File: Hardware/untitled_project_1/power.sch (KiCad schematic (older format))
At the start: 29 parts

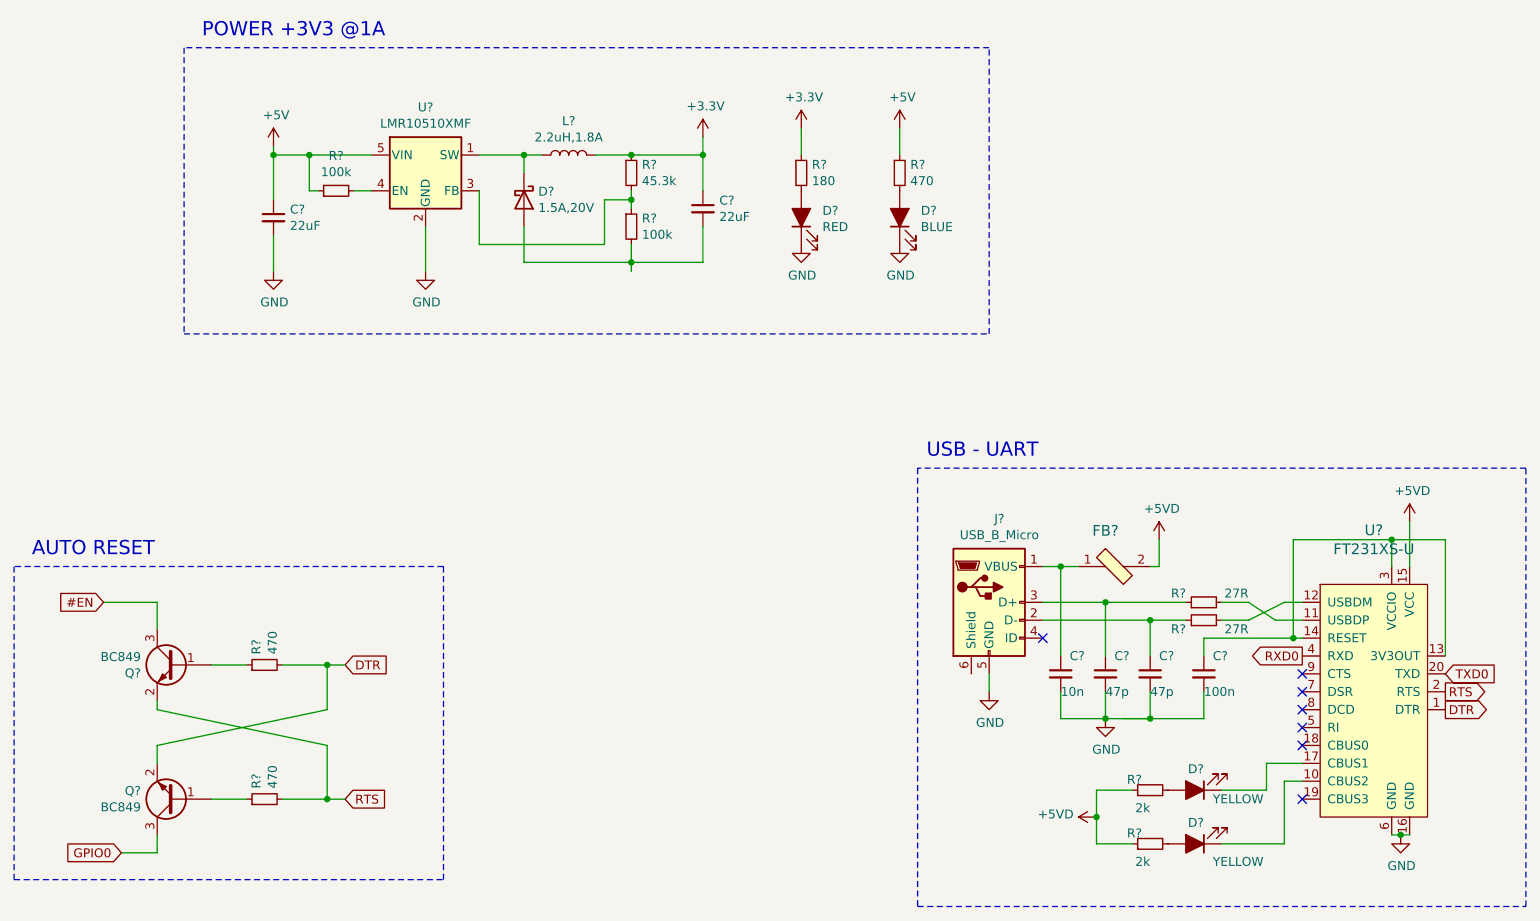
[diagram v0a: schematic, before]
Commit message: add footprints to szymbols:
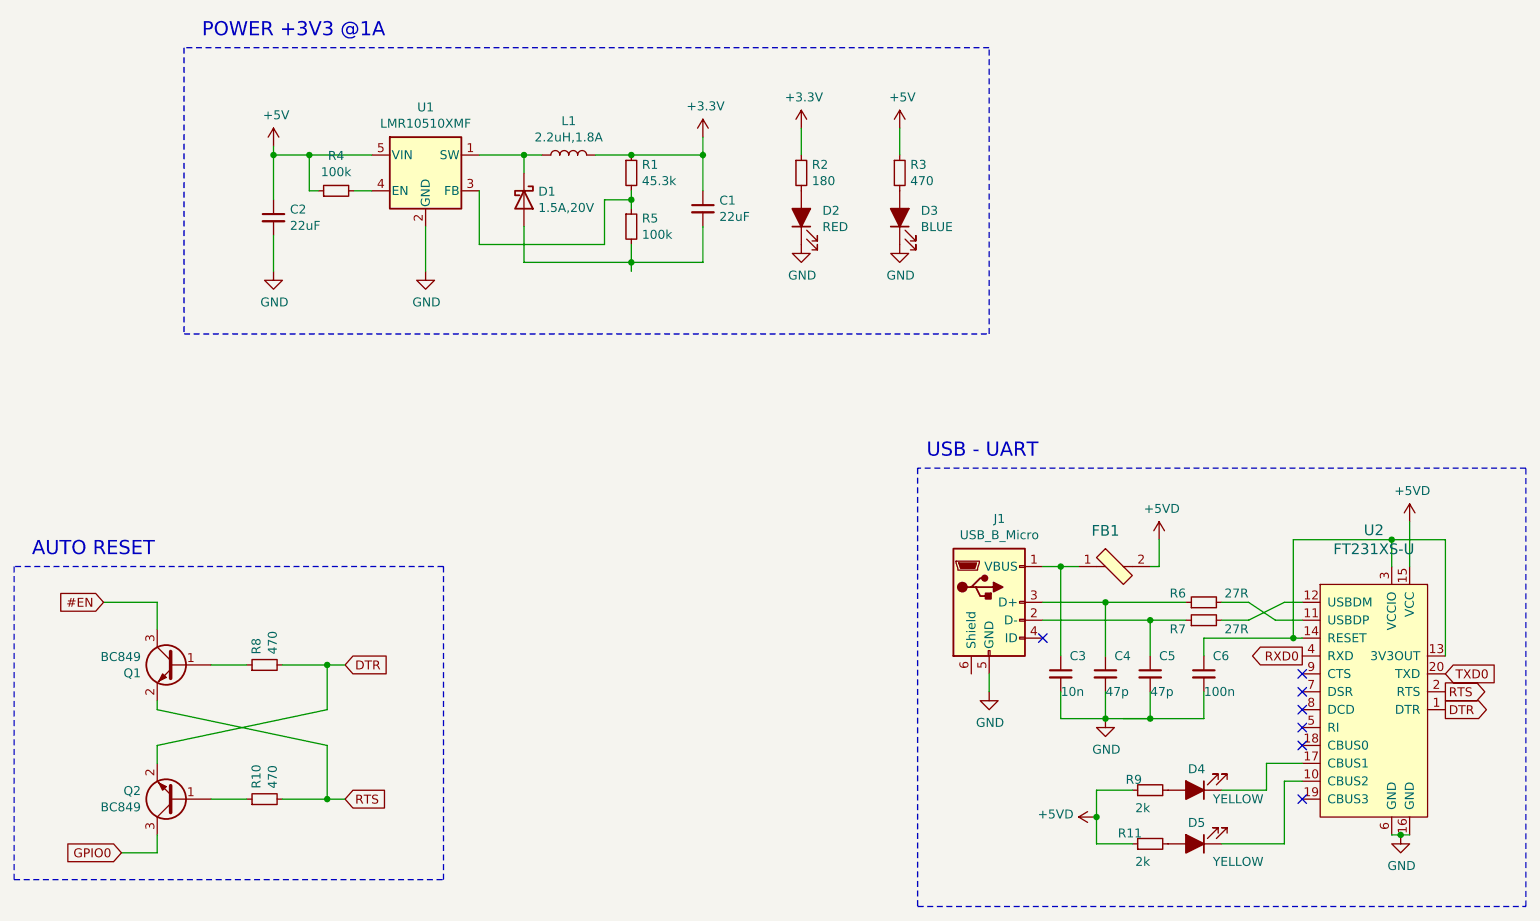
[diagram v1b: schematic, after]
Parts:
- C1, C2, C3, C4, C5, C6: renamed from C?; footprint (none) -> Capacitor_SMD:C_1210_3225Metric_Pad1.42x2.65mm_HandSolder
- D1, D2, D3, D4, D5: renamed from D?; footprint (none) -> Diode_SMD:D_1210_3225Metric_Pad1.42x2.65mm_HandSolder
- FB1: renamed from FB?; footprint digikey-footprints:0805 -> Inductor_SMD:L_0805_2012Metric_Pad1.15x1.40mm_HandSolder
- J1: renamed from J?; footprint (none) -> Connector_USB:USB_Mini-B_Lumberg_2486_01_Horizontal
- L1: renamed from L?; footprint (none) -> Connector_USB:USB_Micro-B_Molex_47346-0001
- R1, R10, R11, R2, R3, R4, R5, R6, R7, R8, R9: renamed from R?; footprint (none) -> Resistor_SMD:R_1210_3225Metric_Pad1.42x2.65mm_HandSolder
- U2: renamed from U?; footprint digikey-footprints:SSOP-20_W3.9mm -> (none)
- gave numbers to parts that had none: 3
